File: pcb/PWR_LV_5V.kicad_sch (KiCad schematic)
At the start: 14 parts, among them IC4 LMR51460SQDRRRQ1

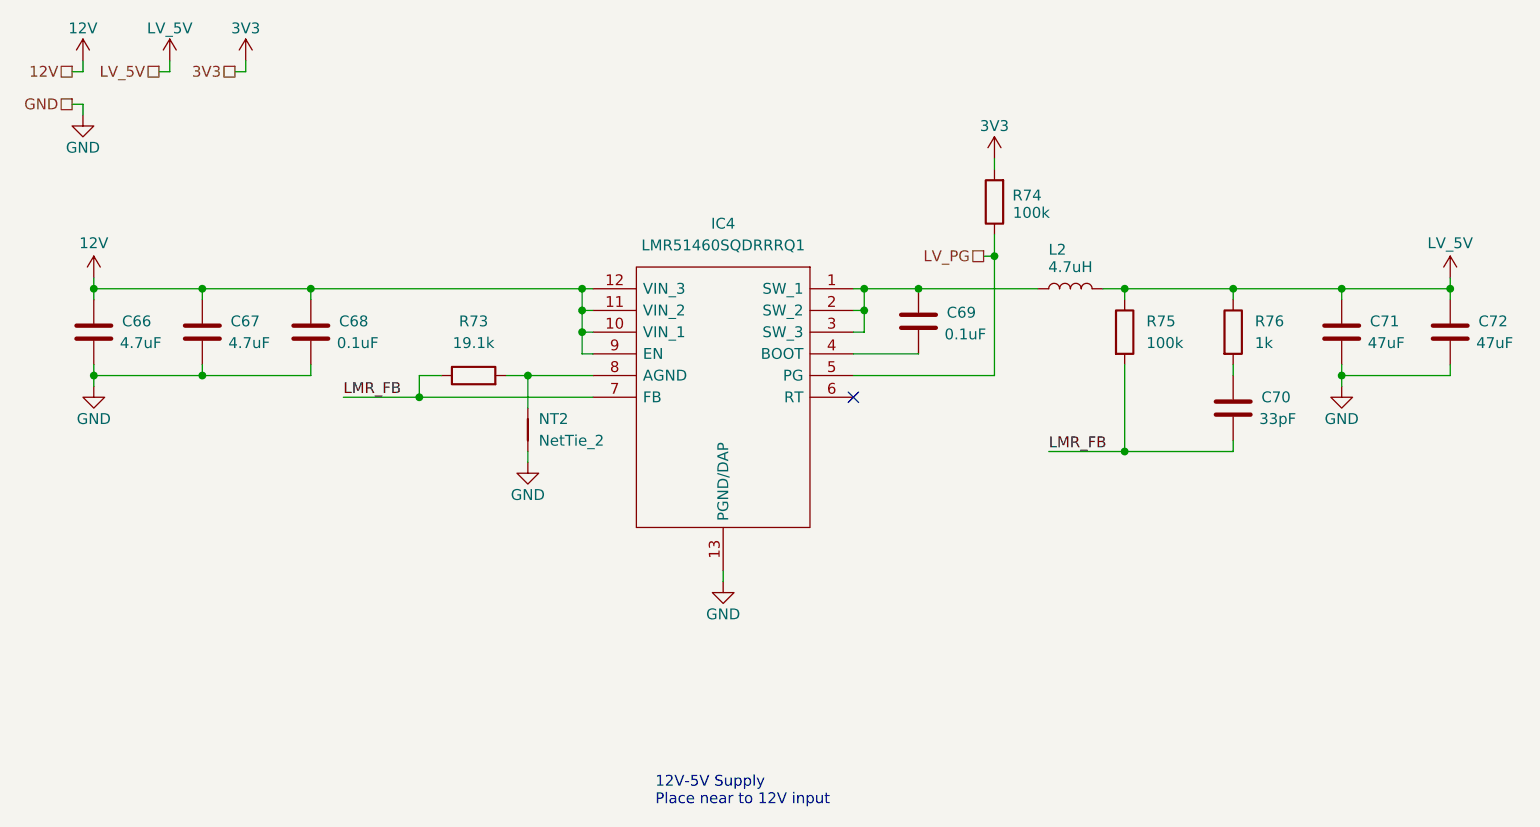
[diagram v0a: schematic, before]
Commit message: reannotated, updated some symbols
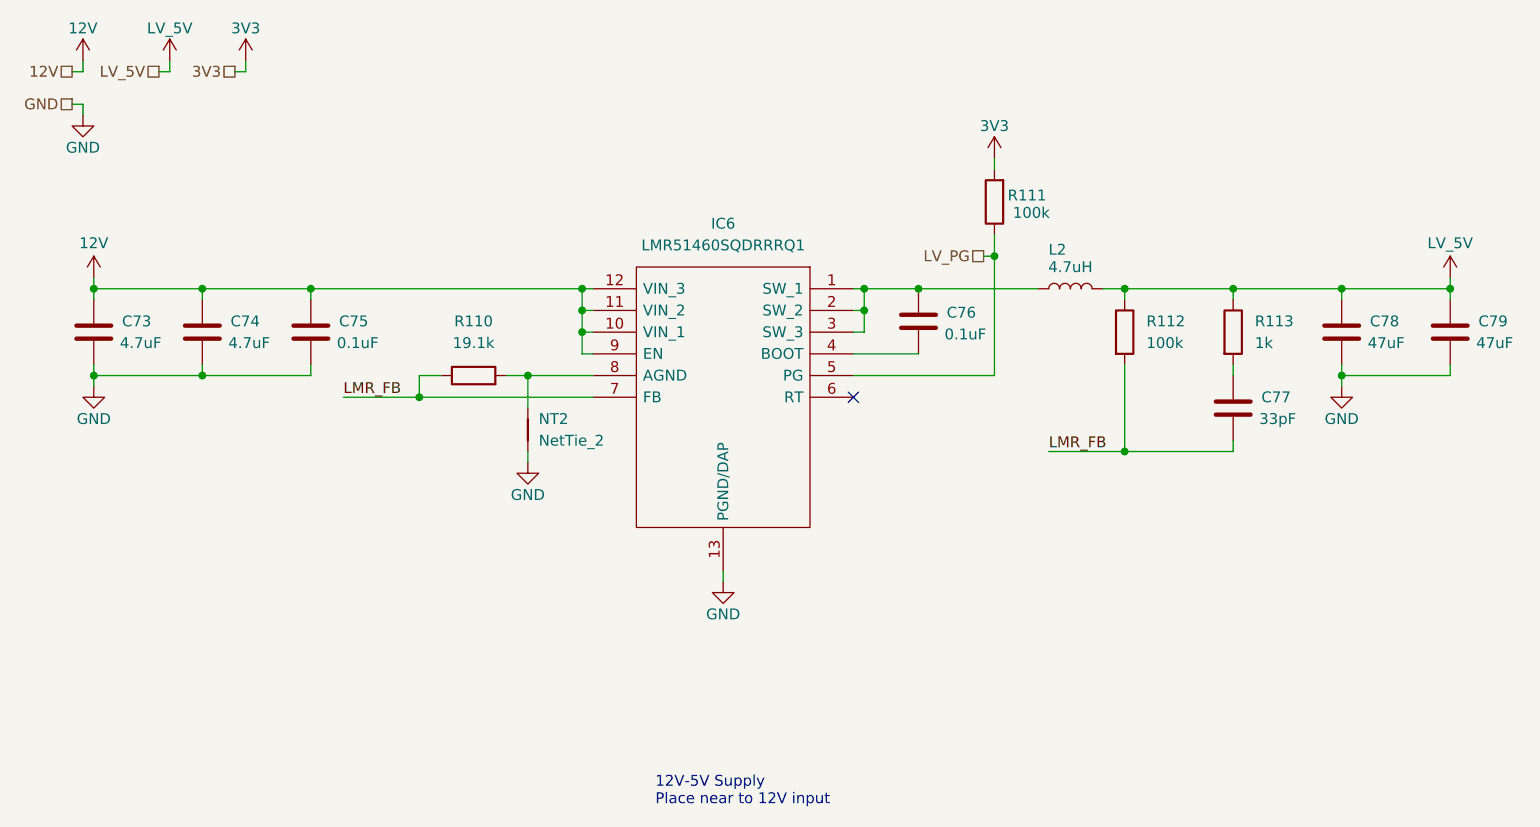
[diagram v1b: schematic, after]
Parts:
- renumbered C66 to C73, C67 to C74, C68 to C75, C69 to C76, C70 to C77, C71 to C78, C72 to C79, IC4 to IC6, R73 to R110, R74 to R111, R75 to R112, R76 to R113
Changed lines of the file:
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@@
 		(dnp no)
 		(fields_autoplaced yes)
-		(property "Reference" "R76"
+		(property "Reference" "R113"
 			(at 161.29 52.0699 0)
 			(effects
@@
 			(project "NCU"
 				(path "/3aee14c3-5480-4f7c-989e-3fef81779034/05e3be97-98f6-4518-a1a7-240d4da327e6/55c548c3-ff9a-4db1-af94-bd7e8aa4e38e"
-					(reference "R76")
+					(reference "R113")
 					(unit 1)
 				)
@@
 		(dnp no)
 		(fields_autoplaced yes)
-		(property "Reference" "R73"
+		(property "Reference" "R110"
 			(at 69.85 52.07 90)
 			(effects
@@
 			(project "NCU"
 				(path "/3aee14c3-5480-4f7c-989e-3fef81779034/05e3be97-98f6-4518-a1a7-240d4da327e6/55c548c3-ff9a-4db1-af94-bd7e8aa4e38e"
-					(reference "R73")
+					(reference "R110")
 					(unit 1)
 				)
@@
 		(on_board yes)
 		(dnp no)
-		(property "Reference" "C67"
+		(property "Reference" "C74"
 			(at 41.402 52.07 0)
 			(effects
@@
 			(project "NCU"
 				(path "/3aee14c3-5480-4f7c-989e-3fef81779034/05e3be97-98f6-4518-a1a7-240d4da327e6/55c548c3-ff9a-4db1-af94-bd7e8aa4e38e"
-					(reference "C67")
+					(reference "C74")
 					(unit 1)
 				)
@@
 		(on_board yes)
 		(dnp no)
-		(property "Reference" "C68"
+		(property "Reference" "C75"
 			(at 54.102 52.07 0)
 			(effects
@@
 			(project "NCU"
 				(path "/3aee14c3-5480-4f7c-989e-3fef81779034/05e3be97-98f6-4518-a1a7-240d4da327e6/55c548c3-ff9a-4db1-af94-bd7e8aa4e38e"
-					(reference "C68")
+					(reference "C75")
 					(unit 1)
 				)
@@
 		(on_board yes)
 		(dnp no)
-		(property "Reference" "C71"
+		(property "Reference" "C78"
 			(at 174.752 52.07 0)
 			(effects
@@
 			(project "NCU"
 				(path "/3aee14c3-5480-4f7c-989e-3fef81779034/05e3be97-98f6-4518-a1a7-240d4da327e6/55c548c3-ff9a-4db1-af94-bd7e8aa4e38e"
-					(reference "C71")
+					(reference "C78")
 					(unit 1)
 				)
@@
 		(on_board yes)
 		(dnp no)
-		(property "Reference" "IC4"
+		(property "Reference" "IC6"
 			(at 99.06 40.64 0)
 			(effects
@@
 			(project "NCU"
 				(path "/3aee14c3-5480-4f7c-989e-3fef81779034/05e3be97-98f6-4518-a1a7-240d4da327e6/55c548c3-ff9a-4db1-af94-bd7e8aa4e38e"
-					(reference "IC4")
+					(reference "IC6")
 					(unit 1)
 				)
@@
 		(on_board yes)
 		(dnp no)
-		(property "Reference" "#PWR0270"
+		(property "Reference" "#PWR0364"
 			(at 76.2 74.93 0)
 			(effects
@@
 			(project "NCU"
 				(path "/3aee14c3-5480-4f7c-989e-3fef81779034/05e3be97-98f6-4518-a1a7-240d4da327e6/55c548c3-ff9a-4db1-af94-bd7e8aa4e38e"
-					(reference "#PWR0270")
+					(reference "#PWR0364")
 					(unit 1)
 				)
@@
 		(dnp no)
 		(fields_autoplaced yes)
-		(property "Reference" "R75"
+		(property "Reference" "R112"
 			(at 148.59 52.0699 0)
 			(effects
@@
 			(project "NCU"
 				(path "/3aee14c3-5480-4f7c-989e-3fef81779034/05e3be97-98f6-4518-a1a7-240d4da327e6/55c548c3-ff9a-4db1-af94-bd7e8aa4e38e"
-					(reference "R75")
+					(reference "R112")
 					(unit 1)
 				)
@@
 		(on_board yes)
 		(dnp no)
-		(property "Reference" "#PWR0273"
+		(property "Reference" "#PWR0367"
 			(at 171.45 66.04 0)
 			(effects
@@
 			(project "NCU"
 				(path "/3aee14c3-5480-4f7c-989e-3fef81779034/05e3be97-98f6-4518-a1a7-240d4da327e6/55c548c3-ff9a-4db1-af94-bd7e8aa4e38e"
-					(reference "#PWR0273")
+					(reference "#PWR0367")
 					(unit 1)
 				)
@@
 		(on_board yes)
 		(dnp no)
-		(property "Reference" "C70"
+		(property "Reference" "C77"
 			(at 162.052 60.96 0)
 			(effects
@@
 			(project "NCU"
 				(path "/3aee14c3-5480-4f7c-989e-3fef81779034/05e3be97-98f6-4518-a1a7-240d4da327e6/55c548c3-ff9a-4db1-af94-bd7e8aa4e38e"
-					(reference "C70")
+					(reference "C77")
 					(unit 1)
 				)
@@
 		(on_board yes)
 		(dnp no)
-		(property "Reference" "#PWR0264"
+		(property "Reference" "#PWR0358"
 			(at 24.13 25.4 0)
 			(effects
@@
 			(project "NCU"
 				(path "/3aee14c3-5480-4f7c-989e-3fef81779034/05e3be97-98f6-4518-a1a7-240d4da327e6/55c548c3-ff9a-4db1-af94-bd7e8aa4e38e"
-					(reference "#PWR0264")
+					(reference "#PWR0358")
 					(unit 1)
 				)
@@
 		(on_board yes)
 		(dnp no)
-		(property "Reference" "C69"
+		(property "Reference" "C76"
 			(at 125.222 51.054 0)
 			(effects
@@
 			(project "NCU"
 				(path "/3aee14c3-5480-4f7c-989e-3fef81779034/05e3be97-98f6-4518-a1a7-240d4da327e6/55c548c3-ff9a-4db1-af94-bd7e8aa4e38e"
-					(reference "C69")
+					(reference "C76")
 					(unit 1)
 				)
@@
 		(on_board yes)
 		(dnp no)
-		(property "Reference" "#PWR0268"
+		(property "Reference" "#PWR0362"
 			(at 34.29 25.4 0)
 			(effects
@@
 			(project "NCU"
 				(path "/3aee14c3-5480-4f7c-989e-3fef81779034/05e3be97-98f6-4518-a1a7-240d4da327e6/55c548c3-ff9a-4db1-af94-bd7e8aa4e38e"
-					(reference "#PWR0268")
+					(reference "#PWR0362")
 					(unit 1)
 				)
@@
 		(on_board yes)
 		(dnp no)
-		(property "Reference" "#PWR0272"
+		(property "Reference" "#PWR0366"
 			(at 130.81 36.83 0)
 			(effects
@@
 			(project "NCU"
 				(path "/3aee14c3-5480-4f7c-989e-3fef81779034/05e3be97-98f6-4518-a1a7-240d4da327e6/55c548c3-ff9a-4db1-af94-bd7e8aa4e38e"
-					(reference "#PWR0272")
+					(reference "#PWR0366")
 					(unit 1)
 				)
@@
 		(on_board yes)
 		(dnp no)
-		(property "Reference" "#PWR0267"
+		(property "Reference" "#PWR0361"
 			(at 25.4 66.04 0)
 			(effects
@@
 			(project "NCU"
 				(path "/3aee14c3-5480-4f7c-989e-3fef81779034/05e3be97-98f6-4518-a1a7-240d4da327e6/55c548c3-ff9a-4db1-af94-bd7e8aa4e38e"
-					(reference "#PWR0267")
+					(reference "#PWR0361")
 					(unit 1)
 				)
@@
 		(on_board yes)
 		(dnp no)
-		(property "Reference" "#PWR0265"
+		(property "Reference" "#PWR0359"
 			(at 24.13 34.29 0)
 			(effects
@@
 			(project "NCU"
 				(path "/3aee14c3-5480-4f7c-989e-3fef81779034/05e3be97-98f6-4518-a1a7-240d4da327e6/55c548c3-ff9a-4db1-af94-bd7e8aa4e38e"
-					(reference "#PWR0265")
+					(reference "#PWR0359")
 					(unit 1)
 				)
@@
 		(on_board yes)
 		(dnp no)
-		(property "Reference" "#PWR0269"
+		(property "Reference" "#PWR0363"
 			(at 43.18 25.4 0)
 			(effects
@@
 			(project "NCU"
 				(path "/3aee14c3-5480-4f7c-989e-3fef81779034/05e3be97-98f6-4518-a1a7-240d4da327e6/55c548c3-ff9a-4db1-af94-bd7e8aa4e38e"
-					(reference "#PWR0269")
+					(reference "#PWR0363")
 					(unit 1)
 				)
@@
 		(on_board yes)
 		(dnp no)
-		(property "Reference" "C66"
+		(property "Reference" "C73"
 			(at 28.702 52.07 0)
 			(effects
@@
 			(project "NCU"
 				(path "/3aee14c3-5480-4f7c-989e-3fef81779034/05e3be97-98f6-4518-a1a7-240d4da327e6/55c548c3-ff9a-4db1-af94-bd7e8aa4e38e"
-					(reference "C66")
+					(reference "C73")
 					(unit 1)
 				)
@@
 		(on_board yes)
 		(dnp no)
-		(property "Reference" "C72"
+		(property "Reference" "C79"
 			(at 187.452 52.07 0)
 			(effects
@@
 			(project "NCU"
 				(path "/3aee14c3-5480-4f7c-989e-3fef81779034/05e3be97-98f6-4518-a1a7-240d4da327e6/55c548c3-ff9a-4db1-af94-bd7e8aa4e38e"
-					(reference "C72")
+					(reference "C79")
 					(unit 1)
 				)
@@
 		(on_board yes)
 		(dnp no)
-		(property "Reference" "#PWR0274"
+		(property "Reference" "#PWR0368"
 			(at 184.15 50.8 0)
 			(effects
@@
 			(project "NCU"
 				(path "/3aee14c3-5480-4f7c-989e-3fef81779034/05e3be97-98f6-4518-a1a7-240d4da327e6/55c548c3-ff9a-4db1-af94-bd7e8aa4e38e"
-					(reference "#PWR0274")
+					(reference "#PWR0368")
 					(unit 1)
 				)
@@
 		(on_board yes)
 		(dnp no)
-		(property "Reference" "#PWR0271"
+		(property "Reference" "#PWR0365"
 			(at 99.06 88.9 0)
 			(effects
@@
 			(project "NCU"
 				(path "/3aee14c3-5480-4f7c-989e-3fef81779034/05e3be97-98f6-4518-a1a7-240d4da327e6/55c548c3-ff9a-4db1-af94-bd7e8aa4e38e"
-					(reference "#PWR0271")
+					(reference "#PWR0365")
 					(unit 1)
 				)
@@
 		(on_board yes)
 		(dnp no)
-		(property "Reference" "R74"
+		(property "Reference" "R111"
 			(at 134.62 37.338 0)
 			(effects
@@
 			(project "NCU"
 				(path "/3aee14c3-5480-4f7c-989e-3fef81779034/05e3be97-98f6-4518-a1a7-240d4da327e6/55c548c3-ff9a-4db1-af94-bd7e8aa4e38e"
-					(reference "R74")
+					(reference "R111")
 					(unit 1)
 				)
@@
 		(on_board yes)
 		(dnp no)
-		(property "Reference" "#PWR0266"
+		(property "Reference" "#PWR0360"
 			(at 25.4 50.8 0)
 			(effects
@@
 			(project "NCU"
 				(path "/3aee14c3-5480-4f7c-989e-3fef81779034/05e3be97-98f6-4518-a1a7-240d4da327e6/55c548c3-ff9a-4db1-af94-bd7e8aa4e38e"
-					(reference "#PWR0266")
-					(unit 1)
-				)
+					(reference "#PWR0360")
+					(unit 1)
+				)

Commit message: 12v input layout done I think
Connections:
- net LMR_SW: now reaches C76.1, IC6.1 (SW_1), IC6.2 (SW_2), IC6.3 (SW_3), L2.1
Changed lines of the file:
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@@
+		)
+	)
+	(label "LMR_SW"
+		(at 114.3 48.26 0)
+		(effects
+			(font
+				(size 1.27 1.27)
+			)
+			(justify left bottom)
 		)
 	)

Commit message: updates from bom release
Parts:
- C73, C74: value 4.7uF -> 4.7u
- C75, C76: value 0.1uF -> 100n
- C77: value 33pF -> 33p
- C78, C79: value 47uF -> 47u
- L2: value 4.7uH -> 4.7u
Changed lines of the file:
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@@
 			)
 		)
-		(property "Value" "4.7uF"
+		(property "Value" "4.7u"
 			(at 41.148 54.61 0)
 			(effects
@@
 			)
 		)
-		(property "Value" "0.1uF"
+		(property "Value" "100n"
 			(at 53.848 54.61 0)
 			(effects
@@
 			)
 		)
-		(property "Value" "47uF"
+		(property "Value" "47u"
 			(at 174.498 54.61 0)
 			(effects
@@
 			)
 		)
-		(property "Value" "4.7uH"
+		(property "Value" "4.7u"
 			(at 139.7 45.72 90)
 			(effects
@@
 			)
 		)
-		(property "Value" "33pF"
+		(property "Value" "33p"
 			(at 161.798 63.5 0)
 			(effects
@@
 			)
 		)
-		(property "Value" "0.1uF"
+		(property "Value" "100n"
 			(at 124.968 53.594 0)
 			(effects
@@
 			)
 		)
-		(property "Value" "4.7uF"
+		(property "Value" "4.7u"
 			(at 28.448 54.61 0)
 			(effects
@@
 			)
 		)
-		(property "Value" "47uF"
+		(property "Value" "47u"
 			(at 187.198 54.61 0)
 			(effects
